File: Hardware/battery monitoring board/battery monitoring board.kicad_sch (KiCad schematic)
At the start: 1 part

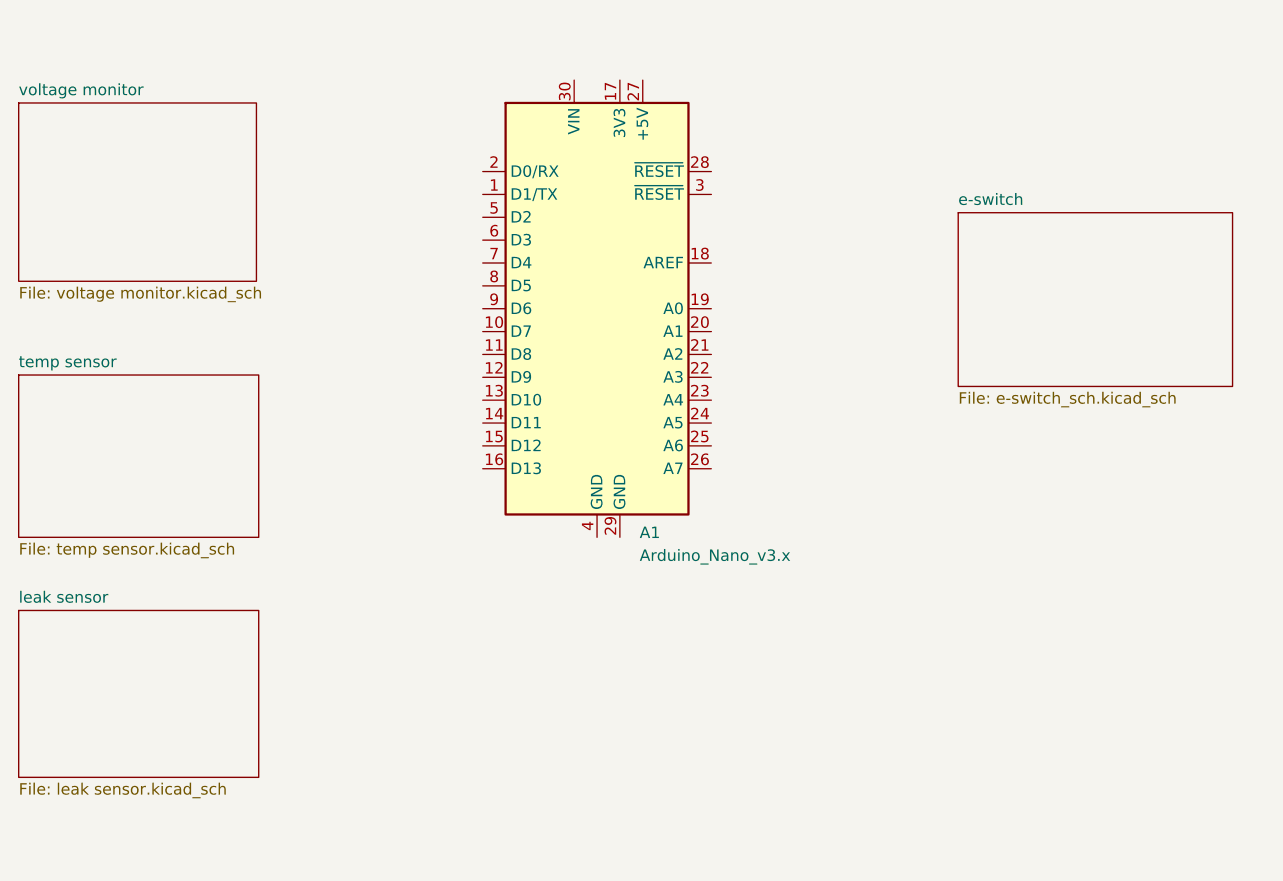
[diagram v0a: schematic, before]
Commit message: added sheet connections to root
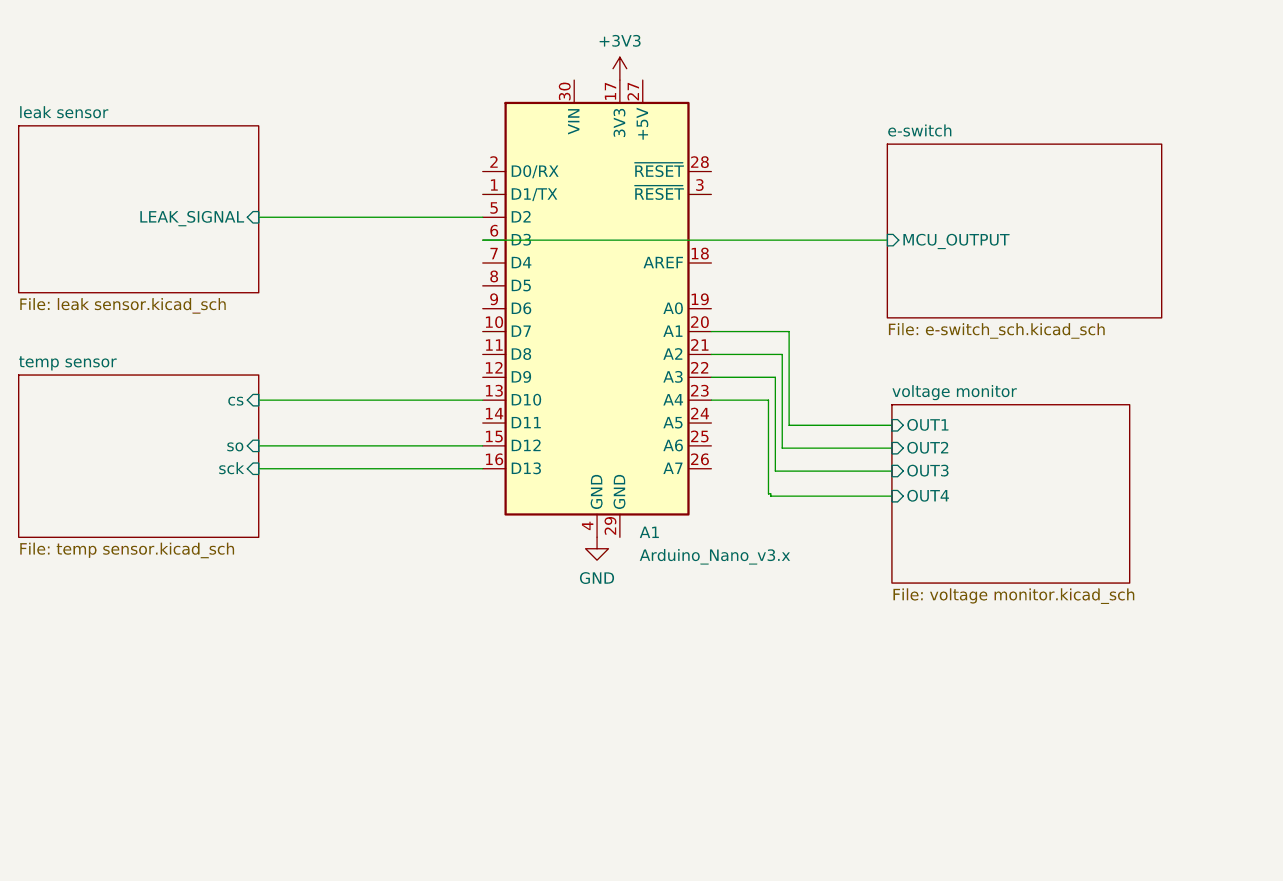
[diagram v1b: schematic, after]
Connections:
- net temp sensor/cs: now reaches A1.13 (D10)
- net temp sensor/so: now reaches A1.15 (D12)
- net temp sensor/sck: now reaches A1.16 (D13)
- net +3V3: now reaches A1.17 (3V3)
- net voltage monitor/OUT1: now reaches A1.20 (A1)
- net voltage monitor/OUT2: now reaches A1.21 (A2)
- net voltage monitor/OUT3: now reaches A1.22 (A3)
- net voltage monitor/OUT4: now reaches A1.23 (A4)
- net GND: now reaches A1.4 (GND)
- net leak sensor/LEAK_SIGNAL: now reaches A1.5 (D2)
- net e-switch/MCU_OUTPUT: now reaches A1.6 (D3)
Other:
- sheet e-switch ports: added MCU_OUTPUT; removed none
- sheet leak sensor ports: added LEAK_SIGNAL; removed none
- sheet temp sensor ports: added cs, sck, so; removed none
- sheet voltage monitor ports: added OUT1, OUT2, OUT3, OUT4; removed none
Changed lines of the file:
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@@
 (kicad_sch (version 20230121) (generator eeschema)
   (paper "A4")
+  (wire (pts (xy 154.178 103.632) (xy 141.224 103.632))
+    (stroke (width 0) (type default))
+  )
+  (wire (pts (xy 83.82 103.378) (xy 108.712 103.378))
+    (stroke (width 0) (type default))
+  )
+  (wire (pts (xy 140.462 106.172) (xy 140.462 95.758))
+    (stroke (width 0) (type default))
+  )
+  (wire (pts (xy 154.178 101.092) (xy 141.986 101.092))
+    (stroke (width 0) (type default))
+  )
+  (wire (pts (xy 141.986 101.092) (xy 141.986 90.678))
+    (stroke (width 0) (type default))
+  )
+  (wire (pts (xy 141.224 93.218) (xy 134.112 93.218))
+    (stroke (width 0) (type default))
+  )
+  (wire (pts (xy 140.716 106.426) (xy 154.178 106.426))
+    (stroke (width 0) (type default))
+  )
+  (wire (pts (xy 134.112 95.758) (xy 140.462 95.758))
+    (stroke (width 0) (type default))
+  )
+  (wire (pts (xy 83.82 95.758) (xy 108.712 95.758))
+    (stroke (width 0) (type default))
+  )
+  (wire (pts (xy 154.178 98.552) (xy 142.748 98.552))
+    (stroke (width 0) (type default))
+  )
+  (wire (pts (xy 108.712 77.978) (xy 153.67 77.978))
+    (stroke (width 0) (type default))
+  )
+  (wire (pts (xy 140.716 106.172) (xy 140.462 106.172))
+    (stroke (width 0) (type default))
+  )
+  (wire (pts (xy 141.224 103.632) (xy 141.224 93.218))
+    (stroke (width 0) (type default))
+  )
+  (wire (pts (xy 142.748 98.552) (xy 142.748 88.138))
+    (stroke (width 0) (type default))
+  )
+  (wire (pts (xy 140.716 106.172) (xy 140.716 106.426))
+    (stroke (width 0) (type default))
+  )
+  (wire (pts (xy 83.82 75.438) (xy 108.712 75.438))
+    (stroke (width 0) (type default))
+  )
+  (wire (pts (xy 142.748 88.138) (xy 134.112 88.138))
+    (stroke (width 0) (type default))
+  )
+  (wire (pts (xy 83.82 100.838) (xy 108.712 100.838))
+    (stroke (width 0) (type default))
+  )
+  (wire (pts (xy 141.986 90.678) (xy 134.112 90.678))
+    (stroke (width 0) (type default))
+  )
   (symbol (lib_id "MCU_Module:Arduino_Nano_v3.x") (at 121.412 85.598 0) (unit 1)
     (in_bom yes) (on_board yes) (dnp no) (fields_autoplaced)
@@
     )
   )
+  (symbol (lib_id "PCM_4ms_Power-symbol:GND") (at 121.412 110.998 0) (unit 1)
+    (in_bom yes) (on_board yes) (dnp no) (fields_autoplaced)
+    (property "Reference" "#PWR01" (at 121.412 117.348 0)
+      (effects (font (size 1.27 1.27)) hide)
+    )
+    (property "Value" "GND" (at 121.412 115.57 0)
+      (effects (font (size 1.27 1.27)))
+    )
+    (property "Footprint" "" (at 121.412 110.998 0)
+      (effects (font (size 1.27 1.27)) hide)
+    )
+    (property "Datasheet" "" (at 121.412 110.998 0)
+      (effects (font (size 1.27 1.27)) hide)
+    )
+    (pin "1")
+    (instances
+      (project "battery monitoring board"
+        (path "/bf623d80-ca5a-491f-9daa-4dffbeba5279"
+          (reference "#PWR01") (unit 1)
+        )
+      )
+    )
+  )
+  (symbol (lib_id "power:+3V3") (at 123.952 60.198 0) (unit 1)
+    (in_bom yes) (on_board yes) (dnp no) (fields_autoplaced)
+    (property "Reference" "#PWR02" (at 123.952 64.008 0)
+      (effects (font (size 1.27 1.27)) hide)
+    )
+    (property "Value" "+3V3" (at 123.952 55.88 0)
+      (effects (font (size 1.27 1.27)))
+    )
+    (property "Footprint" "" (at 123.952 60.198 0)
+      (effects (font (size 1.27 1.27)) hide)
+    )
+    (property "Datasheet" "" (at 123.952 60.198 0)
+      (effects (font (size 1.27 1.27)) hide)
+    )
+    (pin "1")
+    (instances
+      (project "battery monitoring board"
+        (path "/bf623d80-ca5a-491f-9daa-4dffbeba5279"
+          (reference "#PWR02") (unit 1)
+        )
+      )
+    )
+  )
   (sheet (at 57.15 92.964) (size 26.67 18.034) (fields_autoplaced)
     (stroke (width 0.1524) (type solid))
@@
       (effects (font (size 1.27 1.27)) (justify left top))
     )
+    (pin "sck" input (at 83.82 103.378 0)
+      (effects (font (size 1.27 1.27)) (justify right))
+    )
+    (pin "so" input (at 83.82 100.838 0)
+      (effects (font (size 1.27 1.27)) (justify right))
+    )
+    (pin "cs" input (at 83.82 95.758 0)
+      (effects (font (size 1.27 1.27)) (justify right))
+    )
     (instances
       (project "battery monitoring board"
@@
     )
   )
-  (sheet (at 57.15 119.126) (size 26.67 18.542) (fields_autoplaced)
-    (stroke (width 0.1524) (type solid))
-    (fill (color 0 0 0 0.0000))
-    (property "Sheetname" "leak sensor" (at 57.15 118.4144 0)
-      (effects (font (size 1.27 1.27)) (justify left bottom))
-    )
-    (property "Sheetfile" "leak sensor.kicad_sch" (at 57.15 138.2526 0)
-      (effects (font (size 1.27 1.27)) (justify left top))
+  (sheet (at 57.15 65.278) (size 26.67 18.542) (fields_autoplaced)
+    (stroke (width 0.1524) (type solid))
+    (fill (color 0 0 0 0.0000))
+    (property "Sheetname" "leak sensor" (at 57.15 64.5664 0)
+      (effects (font (size 1.27 1.27)) (justify left bottom))
+    )
+    (property "Sheetfile" "leak sensor.kicad_sch" (at 57.15 84.4046 0)
+      (effects (font (size 1.27 1.27)) (justify left top))
+    )
+    (pin "LEAK_SIGNAL" input (at 83.82 75.438 0)
+      (effects (font (size 1.27 1.27)) (justify right))
     )
     (instances
@@
     )
   )
-  (sheet (at 57.15 62.738) (size 26.416 19.812) (fields_autoplaced)
-    (stroke (width 0.1524) (type solid))
-    (fill (color 0 0 0 0.0000))
-    (property "Sheetname" "voltage monitor" (at 57.15 62.0264 0)
-      (effects (font (size 1.27 1.27)) (justify left bottom))
-    )
-    (property "Sheetfile" "voltage monitor.kicad_sch" (at 57.15 83.1346 0)
-      (effects (font (size 1.27 1.27)) (justify left top))
+  (sheet (at 154.178 96.266) (size 26.416 19.812) (fields_autoplaced)
+    (stroke (width 0.1524) (type solid))
+    (fill (color 0 0 0 0.0000))
+    (property "Sheetname" "voltage monitor" (at 154.178 95.5544 0)
+      (effects (font (size 1.27 1.27)) (justify left bottom))
+    )
+    (property "Sheetfile" "voltage monitor.kicad_sch" (at 154.178 116.6626 0)
+      (effects (font (size 1.27 1.27)) (justify left top))
+    )
+    (pin "OUT4" input (at 154.178 106.426 180)
+      (effects (font (size 1.27 1.27)) (justify left))
+    )
+    (pin "OUT3" input (at 154.178 103.632 180)
+      (effects (font (size 1.27 1.27)) (justify left))
+    )
+    (pin "OUT2" input (at 154.178 101.092 180)
+      (effects (font (size 1.27 1.27)) (justify left))
+    )
+    (pin "OUT1" input (at 154.178 98.552 180)
+      (effects (font (size 1.27 1.27)) (justify left))
     )
     (instances
@@
     )
   )
-  (sheet (at 161.544 74.93) (size 30.48 19.304) (fields_autoplaced)
-    (stroke (width 0.1524) (type solid))
-    (fill (color 0 0 0 0.0000))
-    (property "Sheetname" "e-switch" (at 161.544 74.2184 0)
-      (effects (font (size 1.27 1.27)) (justify left bottom))
-    )
-    (property "Sheetfile" "e-switch_sch.kicad_sch" (at 161.544 94.8186 0)
-      (effects (font (size 1.27 1.27)) (justify left top))
-    )
-    (instances
+  (sheet (at 153.67 67.31) (size 30.48 19.304) (fields_autoplaced)
+    (stroke (width 0.1524) (type solid))
+    (fill (color 0 0 0 0.0000))
+    (property "Sheetname" "e-switch" (at 153.67 66.5984 0)
+      (effects (font (size 1.27 1.27)) (justify left bottom))
+    )
+    (property "Sheetfile" "e-switch_sch.kicad_sch" (at 153.67 87.1986 0)
+      (effects (font (size 1.27 1.27)) (justify left top))
+    )
+    (pin "MCU_OUTPUT" input (at 153.67 77.978 180)
+      (effects (font (size 1.27 1.27)) (justify left))
+    )
+    (instances
